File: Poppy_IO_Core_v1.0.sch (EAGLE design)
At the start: 97 parts, among them IC3 ATMEGA2560-16AU, IC6 LP2985-33DBVR, Q1 16MHz, Q2 16MHz, Q3 16MHz, Q4 16MHz, Q5 24MHz, U1 ATmega16u2, U2 MPU-6000, U3 USB2514B-AEZC, U4 ATmega16u2, U5 ATmega16u2, X1 1376408-SLOT_1.8V

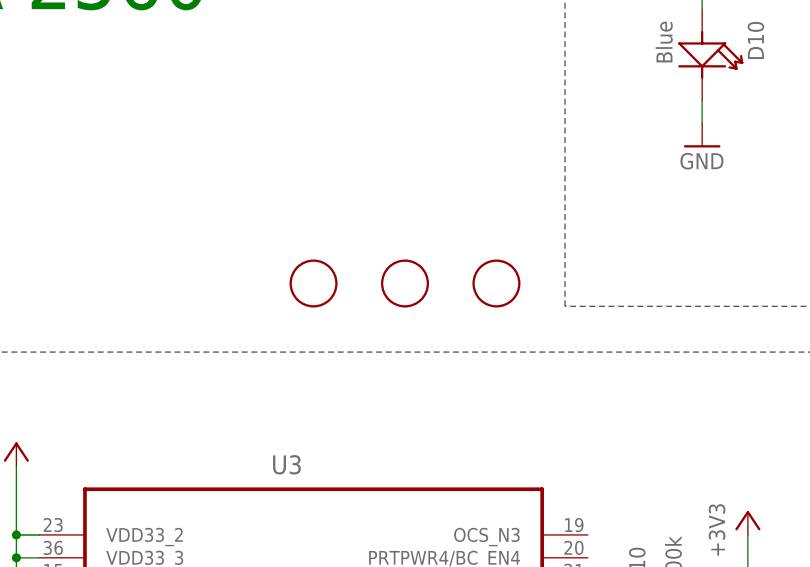
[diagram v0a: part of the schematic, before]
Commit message: Some cosmetic adjustment so that it looks as supposed in circuithub: - removed names and values from the board to hide them (no way to hide the layer!) - removed all solder paste on the back
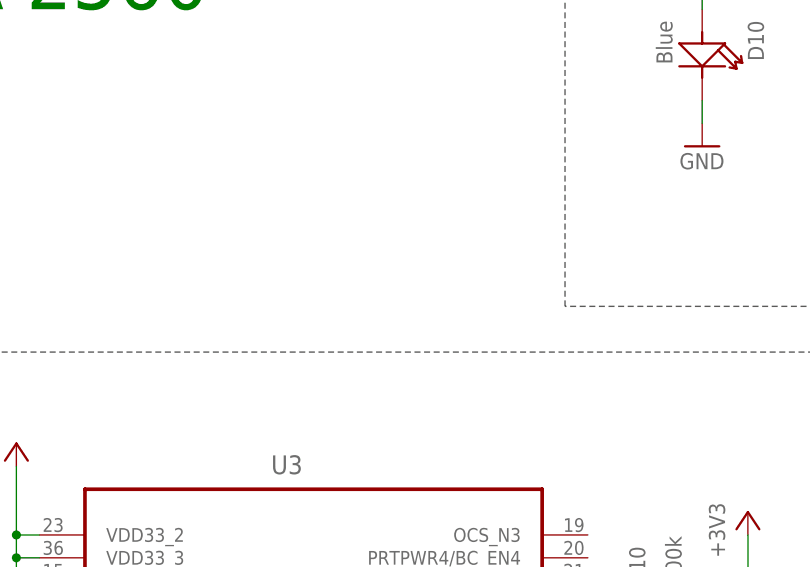
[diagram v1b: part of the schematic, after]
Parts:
- removed FD1, FD2, FD3: FIDUCIALMOUNT, SmartPrj:FIDUCIALMOUNT
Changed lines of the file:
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@@
 <part name="GND15" library="supply1" deviceset="GND" device=""/>
 <part name="P+8" library="supply1" deviceset="+5V" device=""/>
-<part name="FD1" library="SmartPrj" deviceset="FIDUCIALMOUNT" device=""/>
-<part name="FD2" library="SmartPrj" deviceset="FIDUCIALMOUNT" device=""/>
-<part name="FD3" library="SmartPrj" deviceset="FIDUCIALMOUNT" device=""/>
 <part name="GND17" library="supply1" deviceset="GND" device=""/>
 <part name="IC3" library="SmartPrj" deviceset="ATMEGA2560" device="AU" technology="2560-16" value="ATMEGA2560-16AU"/>
@@
 <attribute name="VALUE" x="144.145" y="609.6" size="1.778" layer="96" rot="R180"/>
 </instance>
-<instance part="FD1" gate="G$1" x="99.06" y="558.8"/>
-<instance part="FD2" gate="G$1" x="109.22" y="558.8"/>
-<instance part="FD3" gate="G$1" x="119.38" y="558.8"/>
 <instance part="GND17" gate="1" x="314.96" y="525.78" smashed="yes">
 <attribute name="VALUE" x="312.42" y="523.24" size="1.778" layer="96"/>
